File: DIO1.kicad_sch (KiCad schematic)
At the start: 15 parts, among them J8 AUDIO IN/OUT, J8 DIO-1, J8 SW1-5, K1 G6A-274P-ST-US DC12, K2 G6A-274P-ST-US DC12

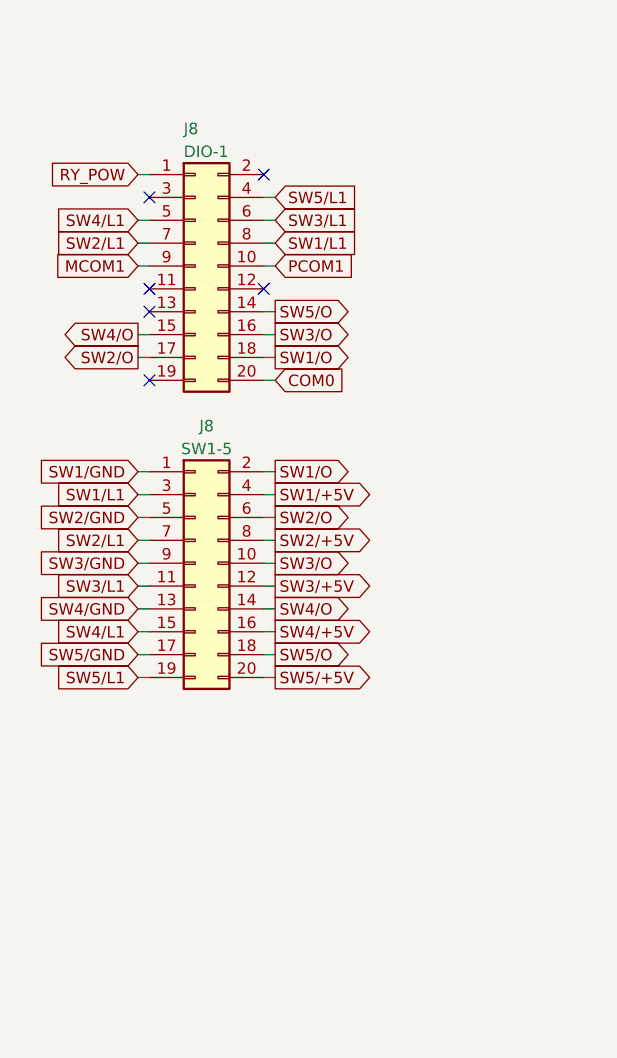
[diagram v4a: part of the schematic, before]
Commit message: SW6/SW7を追加
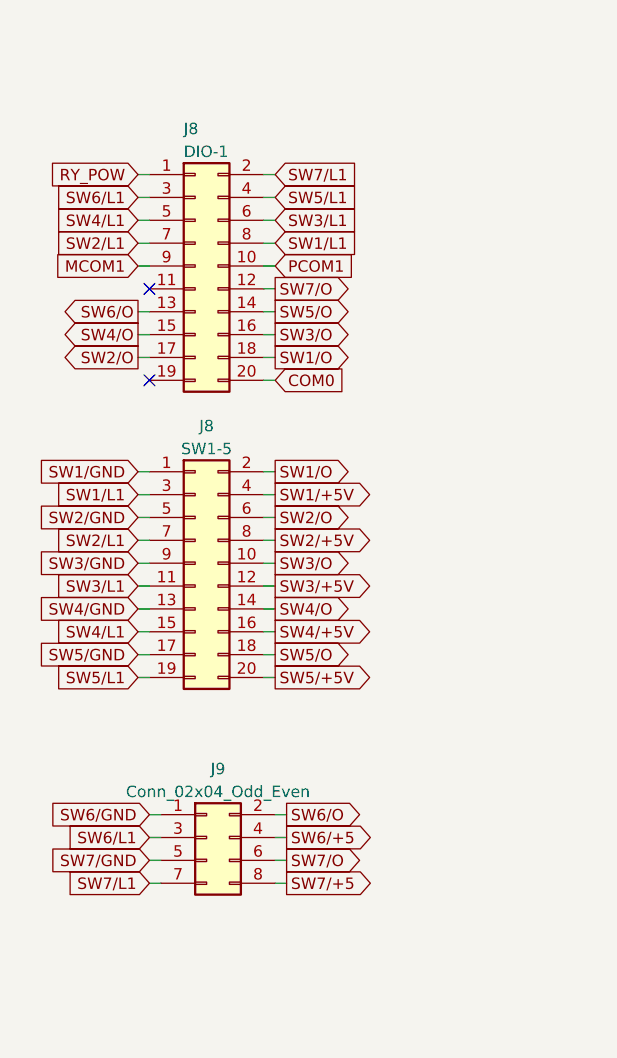
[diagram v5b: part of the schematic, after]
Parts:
- added J9: Conn_02x04_Odd_Even, Connector_PinHeader_2.54mm:PinHeader_2x04_P2.54mm_Vertical, symbol Connector_Generic:Conn_02x04_Odd_Even
- J8: footprint Connector_PinHeader_2.54mm:PinHeader_2x10_P2.54mm_Vertical -> BoxHeader:BoxHeader_2x10_P2.54mm_Vertical
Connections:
- net SW7/O: now reaches J8.12 (Pin_12)
- net SW7/O: now also J9.6 (Pin_6)
- net SW6/O: now reaches J8.13 (Pin_13)
- net SW6/O: now also J9.2 (Pin_2)
- net SW7/L1: now reaches J8.2 (Pin_2)
- net SW7/L1: now also J9.7 (Pin_7)
- net SW6/L1: now reaches J8.3 (Pin_3)
- net SW6/L1: now also J9.3 (Pin_3)
- new net SW6/+5: J9.4 (Pin_4)
- new net SW6/GND: J9.1 (Pin_1)
- new net SW7/+5: J9.8 (Pin_8)
- new net SW7/GND: J9.5 (Pin_5)
- no-connect marks 14 -> 10
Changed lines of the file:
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@@
   (junction (at 209.55 114.3) (diameter 0) (color 0 0 0 0)
   )
-  (no_connect (at 57.15 74.93))
   (no_connect (at 207.01 143.51))
   (no_connect (at 207.01 146.05))
   (no_connect (at 219.71 146.05))
   (no_connect (at 57.15 72.39))
-  (no_connect (at 69.85 59.69))
   (no_connect (at 219.71 151.13))
   (no_connect (at 207.01 151.13))
   (no_connect (at 219.71 143.51))
-  (no_connect (at 69.85 72.39))
-  (no_connect (at 57.15 62.23))
   (no_connect (at 219.71 148.59))
   (no_connect (at 207.01 148.59))
@@
     (stroke (width 0) (type default))
   )
+  (wire (pts (xy 71.12 138.43) (xy 72.39 138.43))
+    (stroke (width 0) (type default))
+  )
   (wire (pts (xy 55.88 102.87) (xy 57.15 102.87))
     (stroke (width 0) (type default))
@@
     (stroke (width 0) (type default))
   )
+  (wire (pts (xy 57.15 133.35) (xy 58.42 133.35))
+    (stroke (width 0) (type default))
+  )
   (wire (pts (xy 248.92 100.33) (xy 255.27 100.33))
     (stroke (width 0) (type default))
@@
     (stroke (width 0) (type default))
   )
+  (wire (pts (xy 69.85 59.69) (xy 71.12 59.69))
+    (stroke (width 0) (type default))
+  )
   (wire (pts (xy 187.96 91.44) (xy 193.04 91.44))
     (stroke (width 0) (type default))
@@
     (stroke (width 0) (type default))
   )
+  (wire (pts (xy 69.85 72.39) (xy 71.12 72.39))
+    (stroke (width 0) (type default))
+  )
   (wire (pts (xy 233.68 39.37) (xy 254 39.37))
     (stroke (width 0) (type default))
@@
     (stroke (width 0) (type default))
   )
+  (wire (pts (xy 57.15 135.89) (xy 58.42 135.89))
+    (stroke (width 0) (type default))
+  )
   (wire (pts (xy 71.12 92.71) (xy 69.85 92.71))
     (stroke (width 0) (type default))
@@
     (stroke (width 0) (type default))
   )
+  (wire (pts (xy 55.88 62.23) (xy 57.15 62.23))
+    (stroke (width 0) (type default))
+  )
   (wire (pts (xy 233.68 44.45) (xy 233.68 53.34))
     (stroke (width 0) (type default))
@@
     (stroke (width 0) (type default))
   )
+  (wire (pts (xy 71.12 133.35) (xy 72.39 133.35))
+    (stroke (width 0) (type default))
+  )
   (wire (pts (xy 71.12 80.01) (xy 69.85 80.01))
     (stroke (width 0) (type default))
   )
+  (wire (pts (xy 57.15 130.81) (xy 58.42 130.81))
+    (stroke (width 0) (type default))
+  )
+  (wire (pts (xy 71.12 130.81) (xy 72.39 130.81))
+    (stroke (width 0) (type default))
+  )
+  (wire (pts (xy 71.12 135.89) (xy 72.39 135.89))
+    (stroke (width 0) (type default))
+  )
   (wire (pts (xy 205.74 36.83) (xy 203.2 36.83))
     (stroke (width 0) (type default))
@@
     (stroke (width 0) (type default))
   )
+  (wire (pts (xy 57.15 138.43) (xy 58.42 138.43))
+    (stroke (width 0) (type default))
+  )
   (wire (pts (xy 201.93 50.8) (xy 201.93 44.45))
     (stroke (width 0) (type default))
@@
     (stroke (width 0) (type default))
   )
+  (wire (pts (xy 55.88 74.93) (xy 57.15 74.93))
+    (stroke (width 0) (type default))
+  )
+  (global_label "SW6{slash}O" (shape output) (at 72.39 130.81 0) (fields_autoplaced)
+    (effects (font (size 1.27 1.27)) (justify left))
+    (property "Intersheetrefs" "${INTERSHEET_REFS}" (at 81.8272 130.81 0)
+      (effects (font (size 1.27 1.27)) (justify left) hide)
+    )
+  )
   (global_label "AUDIO-OUT-L-COLD" (shape output) (at 254 53.34 0) (fields_autoplaced)
     (effects (font (size 1.27 1.27)) (justify left))
@@
     )
   )
+  (global_label "SW7{slash}O" (shape output) (at 71.12 72.39 0) (fields_autoplaced)
+    (effects (font (size 1.27 1.27)) (justify left))
+    (property "Intersheetrefs" "${INTERSHEET_REFS}" (at 80.5572 72.39 0)
+      (effects (font (size 1.27 1.27)) (justify left) hide)
+    )
+  )
+  (global_label "SW7{slash}L1" (shape input) (at 71.12 59.69 0) (fields_autoplaced)
+    (effects (font (size 1.27 1.27)) (justify left))
+    (property "Intersheetrefs" "${INTERSHEET_REFS}" (at 81.4643 59.69 0)
+      (effects (font (size 1.27 1.27)) (justify left) hide)
+    )
+  )
   (global_label "SW2{slash}O" (shape output) (at 71.12 97.79 0) (fields_autoplaced)
     (effects (font (size 1.27 1.27)) (justify left))
@@
     )
   )
+  (global_label "SW6{slash}L1" (shape input) (at 57.15 133.35 180) (fields_autoplaced)
+    (effects (font (size 1.27 1.27)) (justify right))
+    (property "Intersheetrefs" "${INTERSHEET_REFS}" (at 46.8057 133.35 0)
+      (effects (font (size 1.27 1.27)) (justify right) hide)
+    )
+  )
+  (global_label "SW6{slash}+5" (shape output) (at 72.39 133.35 0) (fields_autoplaced)
+    (effects (font (size 1.27 1.27)) (justify left))
+    (property "Intersheetrefs" "${INTERSHEET_REFS}" (at 83.2786 133.35 0)
+      (effects (font (size 1.27 1.27)) (justify left) hide)
+    )
+  )
   (global_label "SW4{slash}L1" (shape input) (at 55.88 110.49 180) (fields_autoplaced)
     (effects (font (size 1.27 1.27)) (justify right))
@@
     )
   )
+  (global_label "SW6{slash}GND" (shape input) (at 57.15 130.81 180) (fields_autoplaced)
+    (effects (font (size 1.27 1.27)) (justify right))
+    (property "Intersheetrefs" "${INTERSHEET_REFS}" (at 45.1728 130.81 0)
+      (effects (font (size 1.27 1.27)) (justify right) hide)
+    )
+  )
+  (global_label "SW7{slash}O" (shape output) (at 72.39 135.89 0) (fields_autoplaced)
+    (effects (font (size 1.27 1.27)) (justify left))
+    (property "Intersheetrefs" "${INTERSHEET_REFS}" (at 81.8272 135.89 0)
+      (effects (font (size 1.27 1.27)) (justify left) hide)
+    )
+  )
   (global_label "SW4{slash}+5V" (shape output) (at 71.12 110.49 0) (fields_autoplaced)
     (effects (font (size 1.27 1.27)) (justify left))
@@
     )
   )
+  (global_label "SW7{slash}+5" (shape output) (at 72.39 138.43 0) (fields_autoplaced)
+    (effects (font (size 1.27 1.27)) (justify left))
+    (property "Intersheetrefs" "${INTERSHEET_REFS}" (at 83.2786 138.43 0)
+      (effects (font (size 1.27 1.27)) (justify left) hide)
+    )
+  )
+  (global_label "SW7{slash}L1" (shape input) (at 57.15 138.43 180) (fields_autoplaced)
+    (effects (font (size 1.27 1.27)) (justify right))
+    (property "Intersheetrefs" "${INTERSHEET_REFS}" (at 46.8057 138.43 0)
+      (effects (font (size 1.27 1.27)) (justify right) hide)
+    )
+  )
   (global_label "SW5{slash}O" (shape output) (at 71.12 74.93 0) (fields_autoplaced)
     (effects (font (size 1.27 1.27)) (justify left))
@@
     )
   )
+  (global_label "SW7{slash}GND" (shape input) (at 57.15 135.89 180) (fields_autoplaced)
+    (effects (font (size 1.27 1.27)) (justify right))
+    (property "Intersheetrefs" "${INTERSHEET_REFS}" (at 45.1728 135.89 0)
+      (effects (font (size 1.27 1.27)) (justify right) hide)
+    )
+  )
   (global_label "SW1{slash}GND" (shape input) (at 55.88 92.71 180) (fields_autoplaced)
     (effects (font (size 1.27 1.27)) (justify right))
@@
     )
   )
+  (global_label "SW6{slash}L1" (shape input) (at 55.88 62.23 180) (fields_autoplaced)
+    (effects (font (size 1.27 1.27)) (justify right))
+    (property "Intersheetrefs" "${INTERSHEET_REFS}" (at 45.5357 62.23 0)
+      (effects (font (size 1.27 1.27)) (justify right) hide)
+    )
+  )
   (global_label "SW3{slash}L1" (shape input) (at 71.12 64.77 0) (fields_autoplaced)
     (effects (font (size 1.27 1.27)) (justify left))
@@
     (property "Intersheetrefs" "${INTERSHEET_REFS}" (at 278.3146 100.33 0)
       (effects (font (size 1.27 1.27)) (justify left) hide)
+    )
+  )
+  (global_label "SW6{slash}O" (shape output) (at 55.88 74.93 180) (fields_autoplaced)
+    (effects (font (size 1.27 1.27)) (justify right))
+    (property "Intersheetrefs" "${INTERSHEET_REFS}" (at 46.4428 74.93 0)
+      (effects (font (size 1.27 1.27)) (justify right) hide)
     )
   )
@@
       (effects (font (size 1.27 1.27)))
     )
-    (property "Footprint" "Connector_PinHeader_2.54mm:PinHeader_2x10_P2.54mm_Vertical" (at 212.09 146.05 0)
+    (property "Footprint" "BoxHeader:BoxHeader_2x10_P2.54mm_Vertical" (at 212.09 146.05 0)
       (effects (font (size 1.27 1.27)) hide)
     )
@@
       (effects (font (size 1.27 1.27)) (justify left))
     )
-    (property "Footprint" "Connector_PinHeader_2.54mm:PinHeader_2x10_P2.54mm_Vertical" (at 62.23 69.85 0)
+    (property "Footprint" "BoxHeader:BoxHeader_2x10_P2.54mm_Vertical" (at 62.23 69.85 0)
       (effects (font (size 1.27 1.27)) hide)
     )
@@
       (effects (font (size 1.27 1.27)))
     )
-    (property "Footprint" "Connector_PinHeader_2.54mm:PinHeader_2x10_P2.54mm_Vertical" (at 62.23 102.87 0)
+    (property "Footprint" "BoxHeader:BoxHeader_2x10_P2.54mm_Vertical" (at 62.23 102.87 0)
       (effects (font (size 1.27 1.27)) hide)
     )
@@
         )
       )
+    )
+  )
+  (symbol (lib_id "Connector_Generic:Conn_02x04_Odd_Even") (at 63.5 133.35 0) (unit 1)
+    (in_bom yes) (on_board yes) (dnp no) (fields_autoplaced)
+    (property "Reference" "J9" (at 64.77 125.73 0)
+      (effects (font (size 1.27 1.27)))
+    )
+    (property "Value" "Conn_02x04_Odd_Even" (at 64.77 128.27 0)
+      (effects (font (size 1.27 1.27)))
+    )
+    (property "Footprint" "Connector_PinHeader_2.54mm:PinHeader_2x04_P2.54mm_Vertical" (at 63.5 133.35 0)
+      (effects (font (size 1.27 1.27)) hide)
+    )
+    (property "Datasheet" "~" (at 63.5 133.35 0)
+      (effects (font (size 1.27 1.27)) hide)
+    )
+    (pin "1")
+    (pin "2")
+    (pin "3")
+    (pin "4")
+    (pin "5")
+    (pin "6")
+    (pin "7")
+    (pin "8")
+    (instances
+      (project "CoughController"
+        (path "/6320cb9c-a8f8-4921-856c-dd9ecac4c251/2e422247-f02f-4cb3-84b7-f23c5e92f071"
+          (reference "J9") (unit 1)
+        )
+      )

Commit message: rename Symbol and Footprint of relay.
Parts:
- K1, K2: value G6A-274P-ST-US DC12 -> G6A-274P-DC5; footprint SnapLibrary:RELAY_G6A-274P-ST-US DC3_OMR -> RELAY_G6A-274P-DC5; symbol G6A-274P-ST-US DC12:G6A-274P-ST-US_DC12 -> G6A-274P-ST-US DC12:G6A-274P-DC5
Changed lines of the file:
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@@
     )
   )
-  (symbol (lib_id "G6A-274P-ST-US DC12:G6A-274P-ST-US_DC12") (at 205.74 86.36 0) (unit 1)
+  (symbol (lib_id "G6A-274P-ST-US DC12:G6A-274P-DC5") (at 205.74 86.36 0) (unit 1)
     (in_bom yes) (on_board yes) (dnp no) (fields_autoplaced)
     (property "Reference" "K2" (at 219.71 77.47 0)
       (effects (font (size 1.524 1.524)))
     )
-    (property "Value" "G6A-274P-ST-US DC12" (at 219.71 80.01 0)
+    (property "Value" "G6A-274P-DC5" (at 219.71 80.01 0)
       (effects (font (size 1.524 1.524)))
     )
-    (property "Footprint" "SnapLibrary:RELAY_G6A-274P-ST-US DC3_OMR" (at 205.74 86.36 0)
+    (property "Footprint" "RELAY_G6A-274P-DC5" (at 205.74 86.36 0)
       (effects (font (size 1.27 1.27) italic) hide)
     )
-    (property "Datasheet" "G6A-274P-ST-US DC12" (at 205.74 86.36 0)
+    (property "Datasheet" "G6A-274P-DC5" (at 205.74 86.36 0)
       (effects (font (size 1.27 1.27) italic) hide)
     )
@@
     )
   )
-  (symbol (lib_id "G6A-274P-ST-US DC12:G6A-274P-ST-US_DC12") (at 205.74 36.83 0) (unit 1)
+  (symbol (lib_id "G6A-274P-ST-US DC12:G6A-274P-DC5") (at 205.74 36.83 0) (unit 1)
     (in_bom yes) (on_board yes) (dnp no) (fields_autoplaced)
     (property "Reference" "K1" (at 219.71 27.94 0)
       (effects (font (size 1.524 1.524)))
     )
-    (property "Value" "G6A-274P-ST-US DC12" (at 219.71 30.48 0)
+    (property "Value" "G6A-274P-DC5" (at 219.71 30.48 0)
       (effects (font (size 1.524 1.524)))
     )
-    (property "Footprint" "SnapLibrary:RELAY_G6A-274P-ST-US DC3_OMR" (at 205.74 36.83 0)
+    (property "Footprint" "RELAY_G6A-274P-DC5" (at 205.74 36.83 0)
       (effects (font (size 1.27 1.27) italic) hide)
     )
-    (property "Datasheet" "G6A-274P-ST-US DC12" (at 205.74 36.83 0)
+    (property "Datasheet" "G6A-274P-DC5" (at 205.74 36.83 0)
       (effects (font (size 1.27 1.27) italic) hide)
     )
